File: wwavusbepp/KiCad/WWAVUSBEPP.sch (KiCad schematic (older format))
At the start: 36 parts, among them J1 USB_B, J2 Conn_01x26_Female, J3 Conn_01x06_Female, J4 Conn_01x04_Male, U1 CY7C68013-56LFC, U2 LT1762-3.3, U3 NCP302LSN45T1G, U4 FM24C64B, Y1 24Mhz

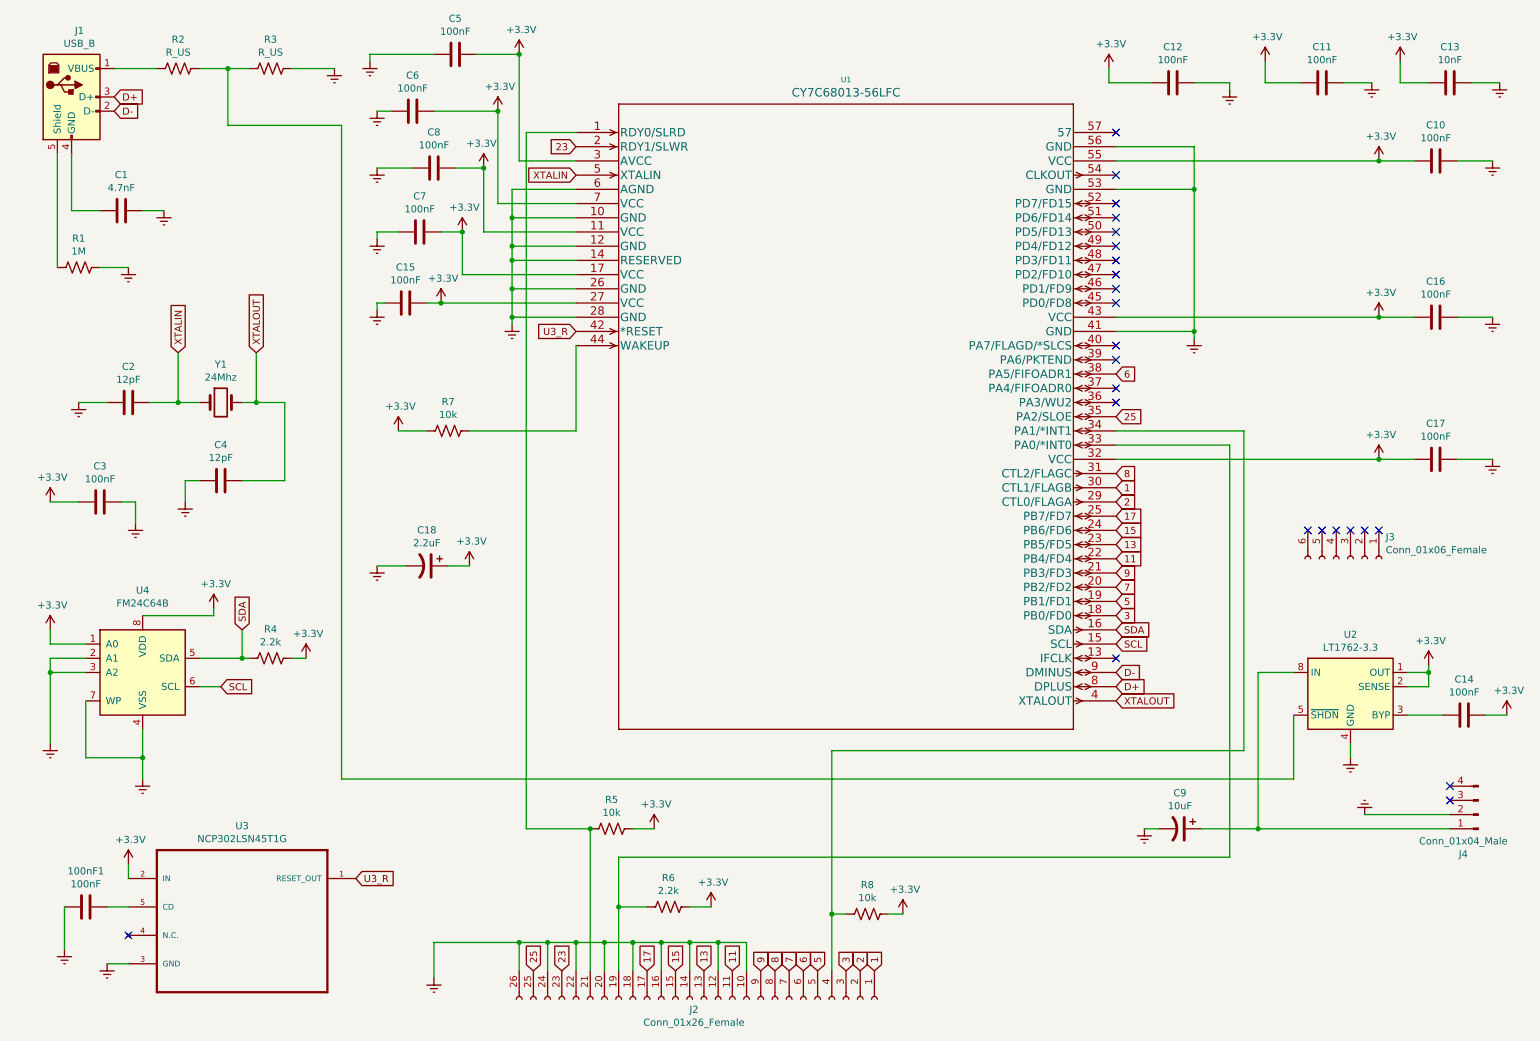
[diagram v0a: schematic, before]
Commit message: Fixes to schematic and renaming components to match website image info.
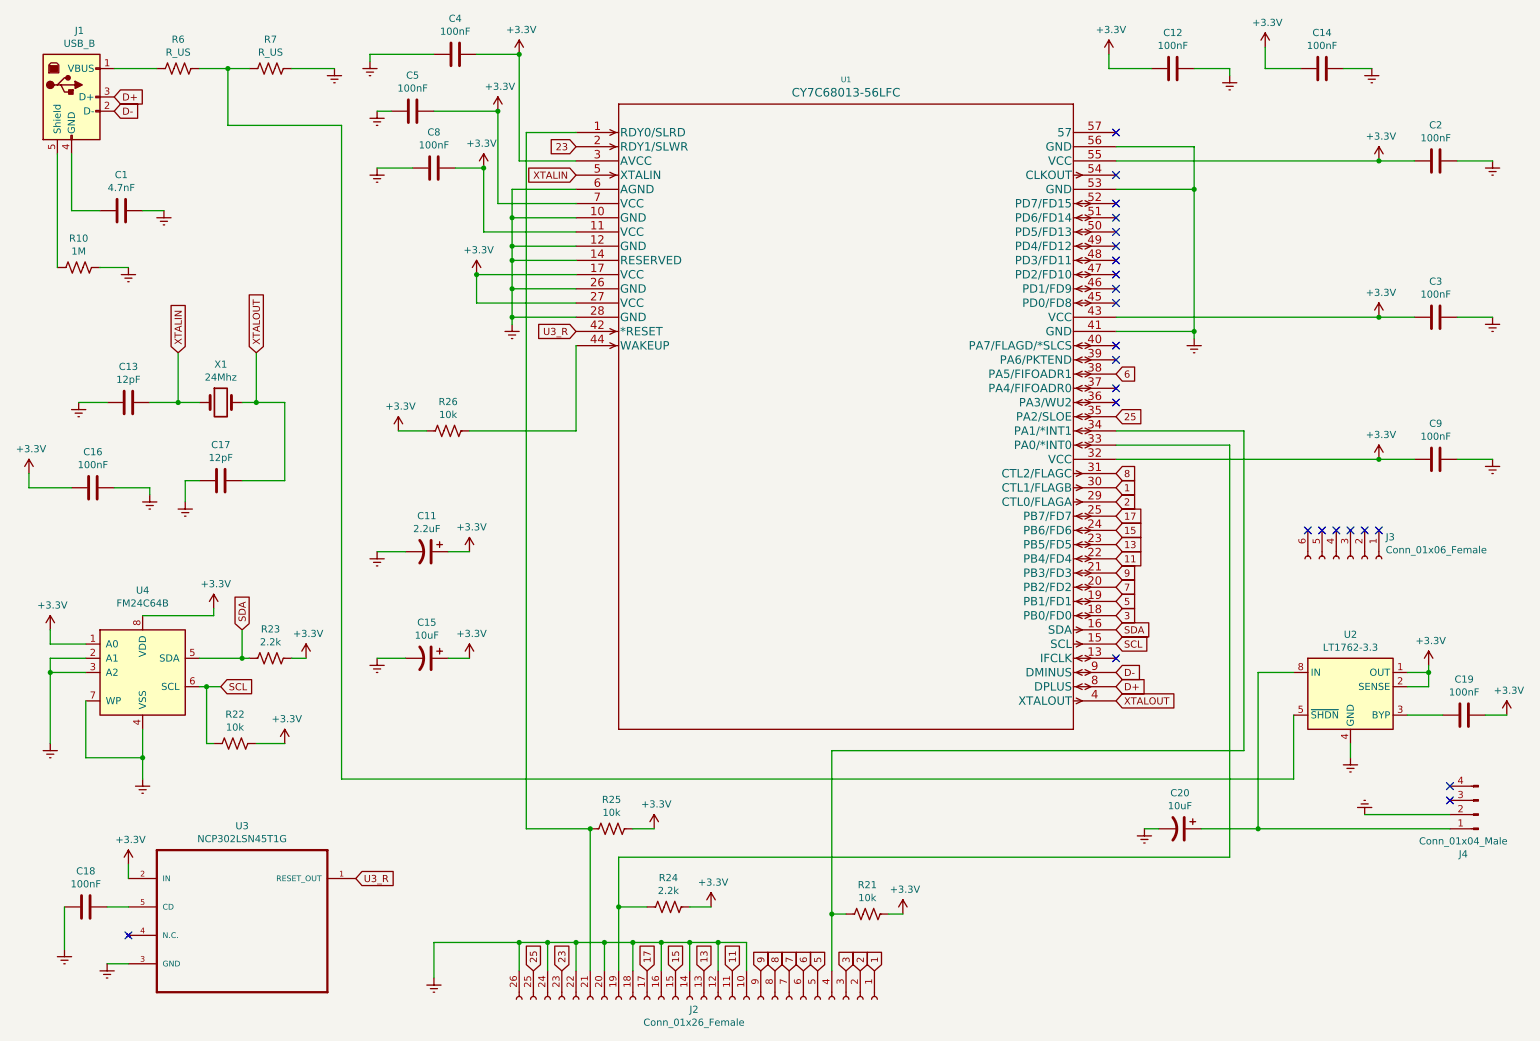
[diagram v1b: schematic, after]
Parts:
- removed C13: 10nF, Capacitor_SMD:C_1206_3216Metric_Pad1.42x1.75mm_HandSolder, symbol Device:C
- removed C15, C3, C7: 100nF, Capacitor_SMD:C_1206_3216Metric_Pad1.42x1.75mm_HandSolder, symbol Device:C
- added C15: 10uF, Capacitor_SMD:C_1206_3216Metric_Pad1.42x1.75mm_HandSolder, symbol Device:CP1
- added C16: 100nF, Capacitor_SMD:C_1206_3216Metric_Pad1.42x1.75mm_HandSolder, symbol Device:C
- added R22: 10k, Resistor_SMD:R_1206_3216Metric_Pad1.42x1.75mm_HandSolder, symbol Device:R_US
- J3: footprint Connector_PinHeader_2.54mm:PinHeader_2x06_P2.54mm_Vertical -> Connector_PinHeader_2.54mm:PinHeader_2x03_P2.54mm_Vertical
- renumbered C18 to C11, C2 to C13, C11 to C14, C4 to C17, 100nF1 to C18, C14 to C19, C10 to C2, C9 to C20, C16 to C3, C5 to C4, C6 to C5, C17 to C9, R1 to R10, R8 to R21, R4 to R23, R6 to R24, R5 to R25, R7 to R26, R2 to R6, R3 to R7, Y1 to X1
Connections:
- net +3V3: now also C15.1, C16.2, R22.1
- net Earth: now also C15.2, C16.1
- net SCL: now also R22.2
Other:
- moved on the sheet: C11, C12, C14

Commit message: Fixed one footprint, and restarted traces.
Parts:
- U3: footprint Package_SO:SOT95P275X110-5N -> SOP95P275X110-5N:SOP95P275X110-5N
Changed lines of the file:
@@
 F 0 "U3" H 2150 7370 50  0000 C CNN
 F 1 "NCP302LSN45T1G" H 2150 7279 50  0000 C CNN
-F 2 "Package_SO:SOT95P275X110-5N" H 2150 6800 50  0001 L BNN
+F 2 "SOP95P275X110-5N:SOP95P275X110-5N" H 2150 6800 50  0001 L BNN
 F 3 "Voltage Detector Series with Programmable Delay and Complementary Output 4.5 V, Reset Low" H 2150 6800 50  0001 L BNN
 F 4 "Unavailable" H 2150 6800 50  0001 L BNN "Field4"

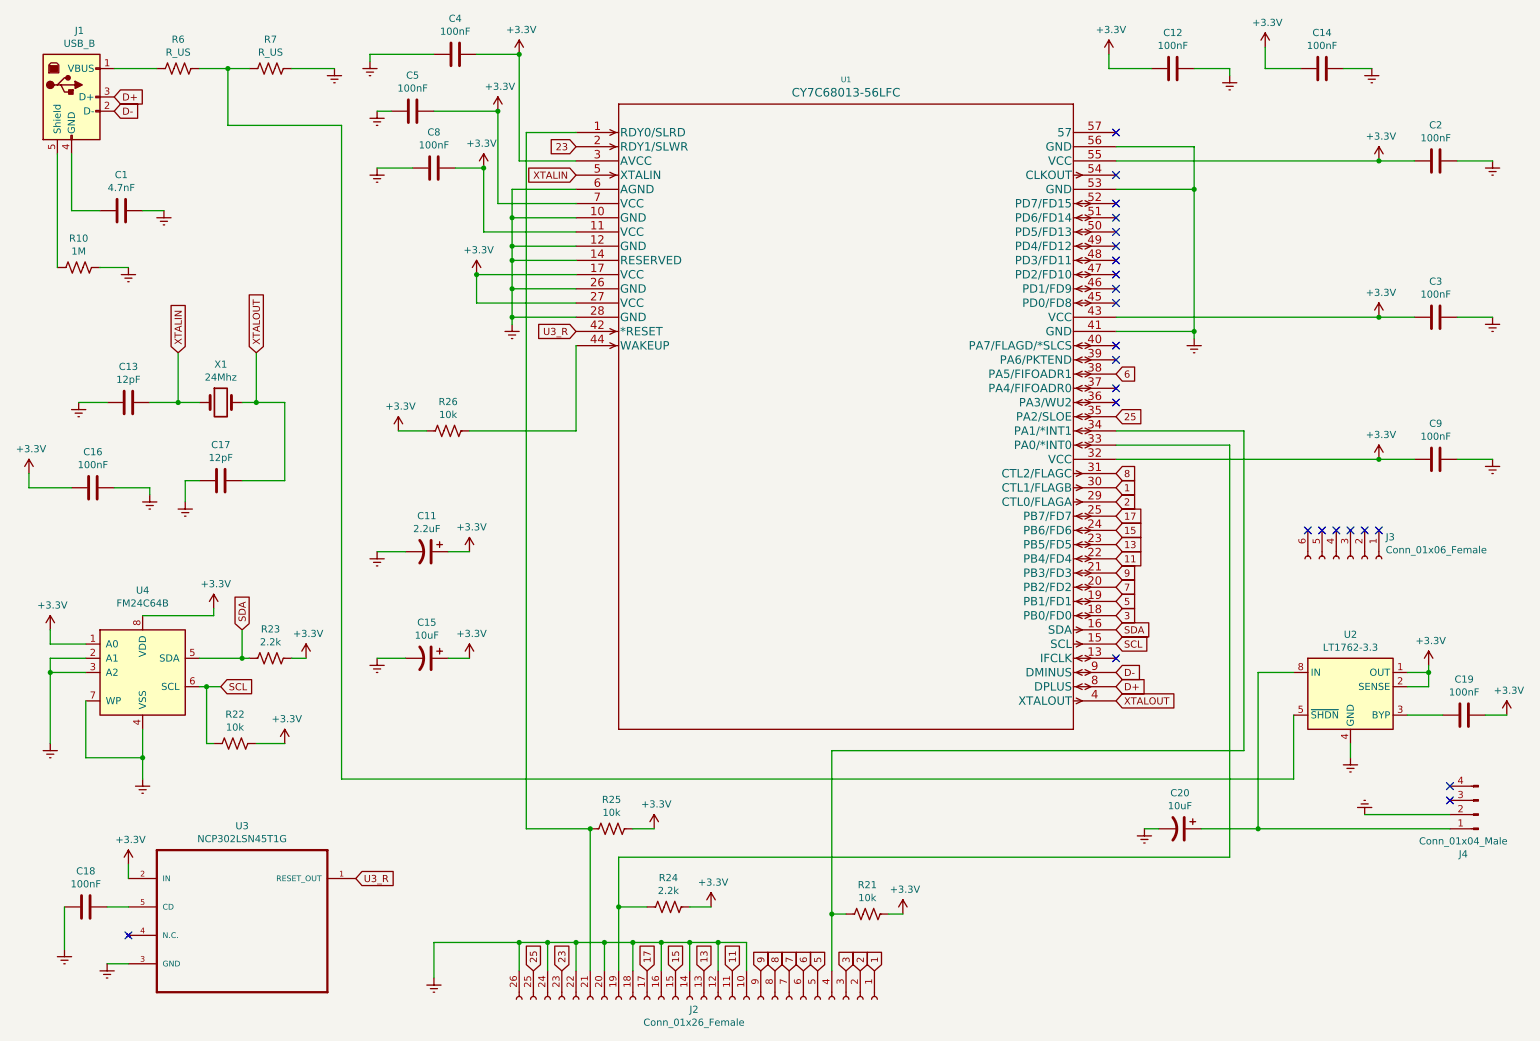
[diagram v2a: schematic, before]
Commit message: Added jumper J5, and fixed some resistor values, and colocated cap next to U4.
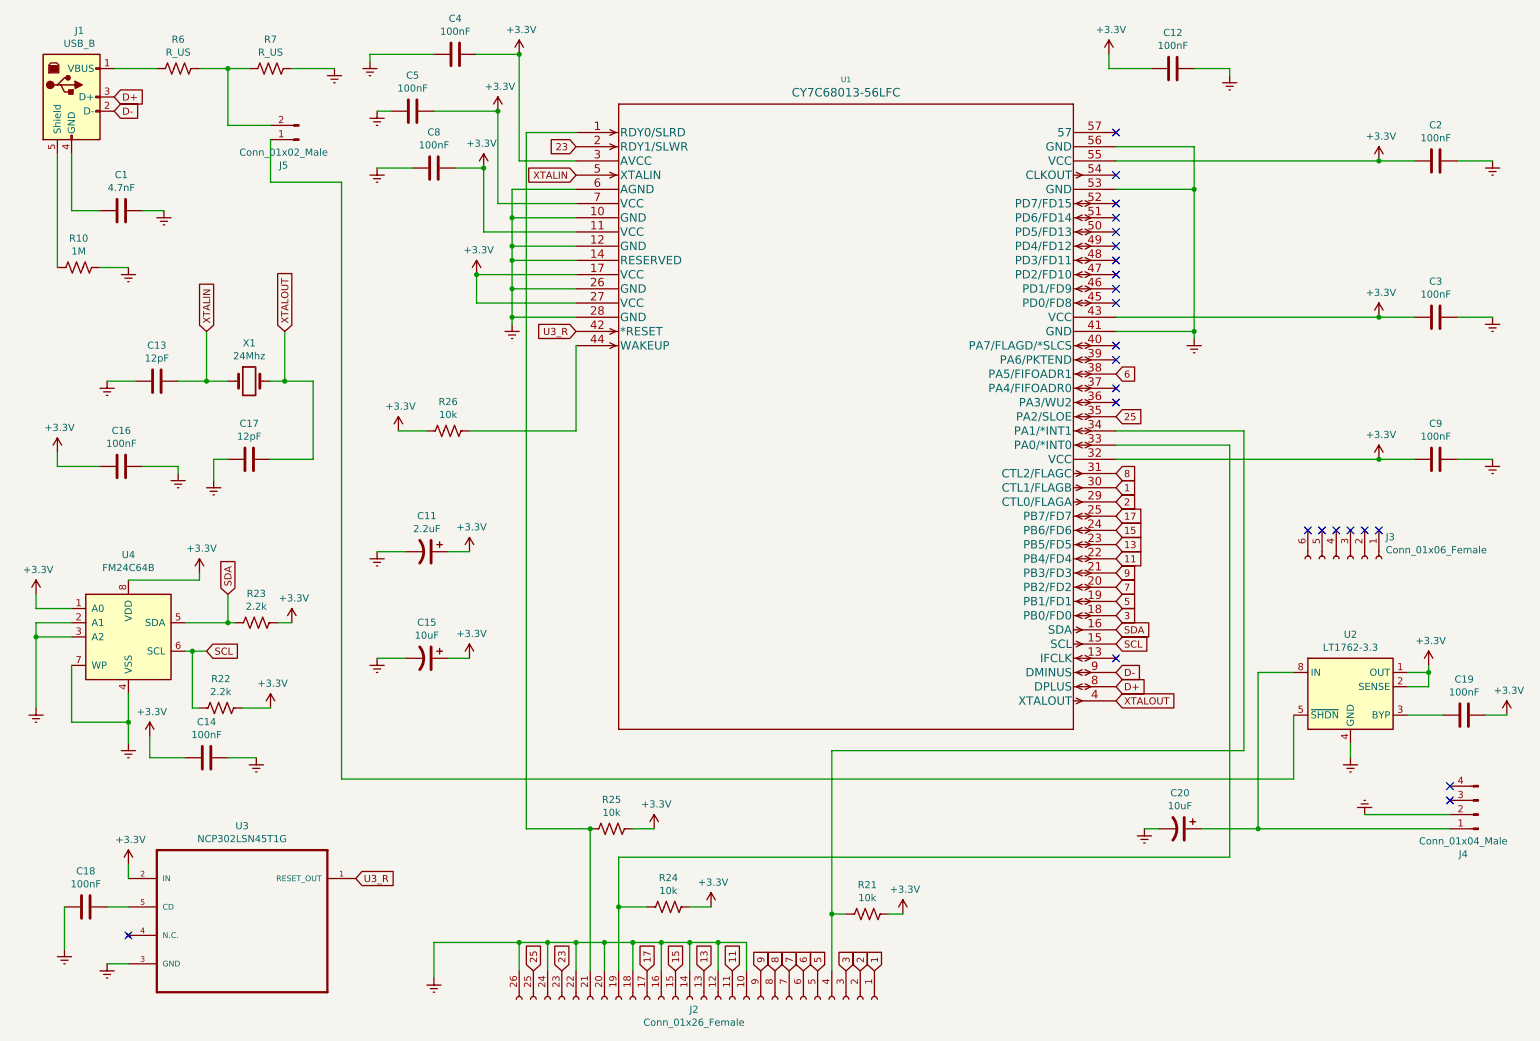
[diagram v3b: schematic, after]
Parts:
- added J5: Conn_01x02_Male, symbol Connector:Conn_01x02_Male
- R22: value 10k -> 2.2k
- R24: value 2.2k -> 10k
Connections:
- net at R6.1, R7.2: now also J5.2 (Pin_2); no longer U2.5 (~SHDN)
- new net: J5.1 (Pin_1), U2.5 (~SHDN)
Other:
- moved on the sheet: C13, C14, C16, C17, R22, R23, U4, X1

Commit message: Added testpoints and rerouted some tracks. Work in progress.
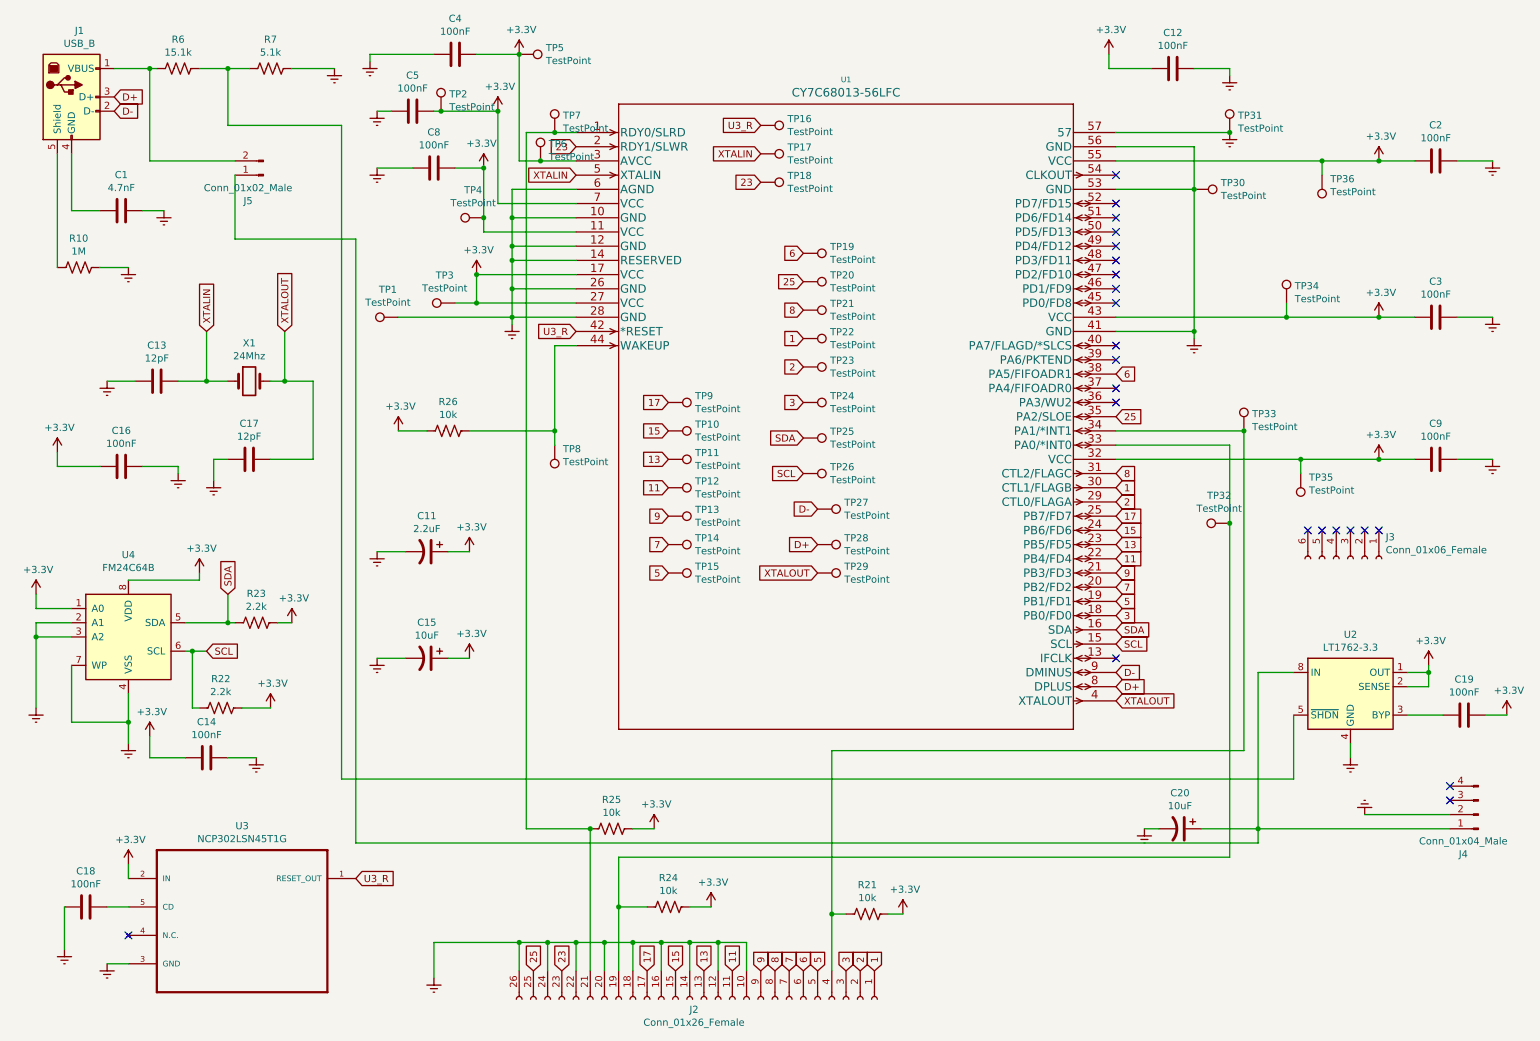
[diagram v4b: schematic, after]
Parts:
- added TP1, TP10, TP11, TP12, TP13, TP14, TP15, TP16, TP17, TP18, TP19, TP2, TP20, TP21, TP22, TP23, TP24, TP25, TP26, TP27, TP28, TP29, TP3, TP30, TP31, TP32, TP33, TP34, TP35, TP36, TP4, TP5, TP6, TP7, TP8, TP9: TestPoint, TestPoint:TestPoint_Pad_1.0x1.0mm, symbol Connector:TestPoint
- C1, C12, C13, C14, C16, C17, C18, C19, C2, C3, C4, C5, C8, C9: footprint Capacitor_SMD:C_1206_3216Metric_Pad1.42x1.75mm_HandSolder -> Capacitor_SMD:C_0805_2012Metric_Pad1.15x1.40mm_HandSolder
- J5: footprint (none) -> Connector_PinHeader_1.00mm:PinHeader_1x02_P1.00mm_Vertical
- R10: footprint Resistor_SMD:R_4020_10251Metric_Pad1.65x5.30mm_HandSolder -> Resistor_SMD:R_0805_2012Metric_Pad1.15x1.40mm_HandSolder
- R21, R22, R23, R24, R25, R26: footprint Resistor_SMD:R_1206_3216Metric_Pad1.42x1.75mm_HandSolder -> Resistor_SMD:R_0805_2012Metric_Pad1.15x1.40mm_HandSolder
- R6: value R_US -> 15.1k; footprint Resistor_SMD:R_1206_3216Metric_Pad1.42x1.75mm_HandSolder -> Resistor_SMD:R_0805_2012Metric_Pad1.15x1.40mm_HandSolder
- R7: value R_US -> 5.1k; footprint Resistor_SMD:R_1206_3216Metric_Pad1.42x1.75mm_HandSolder -> Resistor_SMD:R_0805_2012Metric_Pad1.15x1.40mm_HandSolder
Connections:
- net +3V3: now also TP2.1, TP3.1, TP34.1, TP35.1, TP36.1, TP4.1, TP5.1, TP6.1
- net 1: now also TP22.1
- net 11: now also TP12.1
- net 13: now also TP11.1
- net 15: now also TP10.1
- net 17: now also TP9.1
- net 2: now also TP23.1
- net 23: now also TP18.1
- net 25: now also TP20.1
- net 3: now also TP24.1
- net 5: now also TP15.1
- net 6: now also TP19.1
- net 7: now also TP14.1
- net 8: now also TP21.1
- net 9: now also TP13.1
- net D+: now also TP28.1
- net D-: now also TP27.1
- net Earth: now also U1.57, TP1.1, TP30.1, TP31.1
- net SCL: now also TP26.1
- net SDA: now also TP25.1
- net U3_R: now also TP16.1
- net XTALIN: now also TP17.1
- net XTALOUT: now also TP29.1
- net at U2.5 (~SHDN): now also R6.1, R7.2; no longer J5.1 (Pin_1)
- net at C20.1, J4.1 (Pin_1), U2.8 (IN): now also J5.1 (Pin_1)
- net at J1.1 (VBUS), R6.2: now also J5.2 (Pin_2)
- net at J2.21 (Pin_21), R25.2, U1.1 (RDY0/SLRD): now also TP7.1
- net at J2.19 (Pin_19), R24.2, U1.33 (PA0/*INT0): now also TP32.1
- net at J2.4 (Pin_4), R21.2, U1.34 (PA1/*INT1): now also TP33.1
- net at R26.1, U1.44 (WAKEUP): now also TP8.1
- no-connect marks 24 -> 23
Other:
- moved on the sheet: J5

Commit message: routing complete.
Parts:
- J5: footprint Connector_PinHeader_1.00mm:PinHeader_1x02_P1.00mm_Vertical -> Connector_PinHeader_2.00mm:PinHeader_1x02_P2.00mm_Vertical
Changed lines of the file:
@@
 F 0 "J5" H 2408 1831 50  0000 C CNN
 F 1 "Conn_01x02_Male" H 2408 1740 50  0000 C CNN
-F 2 "Connector_PinHeader_1.00mm:PinHeader_1x02_P1.00mm_Vertical" H 2300 1650 50  0001 C CNN
+F 2 "Connector_PinHeader_2.00mm:PinHeader_1x02_P2.00mm_Vertical" H 2300 1650 50  0001 C CNN
 F 3 "~" H 2300 1650 50  0001 C CNN
 	1    2300 1650

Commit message: Fixed the R10 resistor footprint and rerouting. No silkscreen changes done.
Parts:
- R10: footprint Resistor_SMD:R_0805_2012Metric_Pad1.15x1.40mm_HandSolder -> Resistor_SMD:R_4020_10251Metric_Pad1.65x5.30mm_HandSolder
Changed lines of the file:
@@
 F 0 "R10" V 795 2300 50  0000 C CNN
 F 1 "1M" V 886 2300 50  0000 C CNN
-F 2 "Resistor_SMD:R_0805_2012Metric_Pad1.15x1.40mm_HandSolder" V 1040 2290 50  0001 C CNN
+F 2 "Resistor_SMD:R_4020_10251Metric_Pad1.65x5.30mm_HandSolder" V 1040 2290 50  0001 C CNN
 F 3 "~" H 1000 2300 50  0001 C CNN
 	1    1000 2300
